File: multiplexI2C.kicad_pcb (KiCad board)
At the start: 2 copper layers, 48.3 x 71.1 mm, 59 parts, among them J1 Screw_Terminal_01x04, J17 Conn_01x04_Pin, J18 PinSocket_1x20_P2.54mm_Vertic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, J19 PinSocket_1x20_P2.54mm_Vertic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, J2 Screw_Terminal_01x04, J20 Screw_Terminal_01x02, J3 Screw_Terminal_01x04, J4 Screw_Terminal_01x04, J5 Screw_Terminal_01x04, J6 Screw_Terminal_01x04, J7 Screw_Terminal_01x04, J8 Screw_Terminal_01x04, J9 header_0.25sqmm_1x04_P4.2mm_D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, U1 TCA9548A, U2 RFM95W-915S2

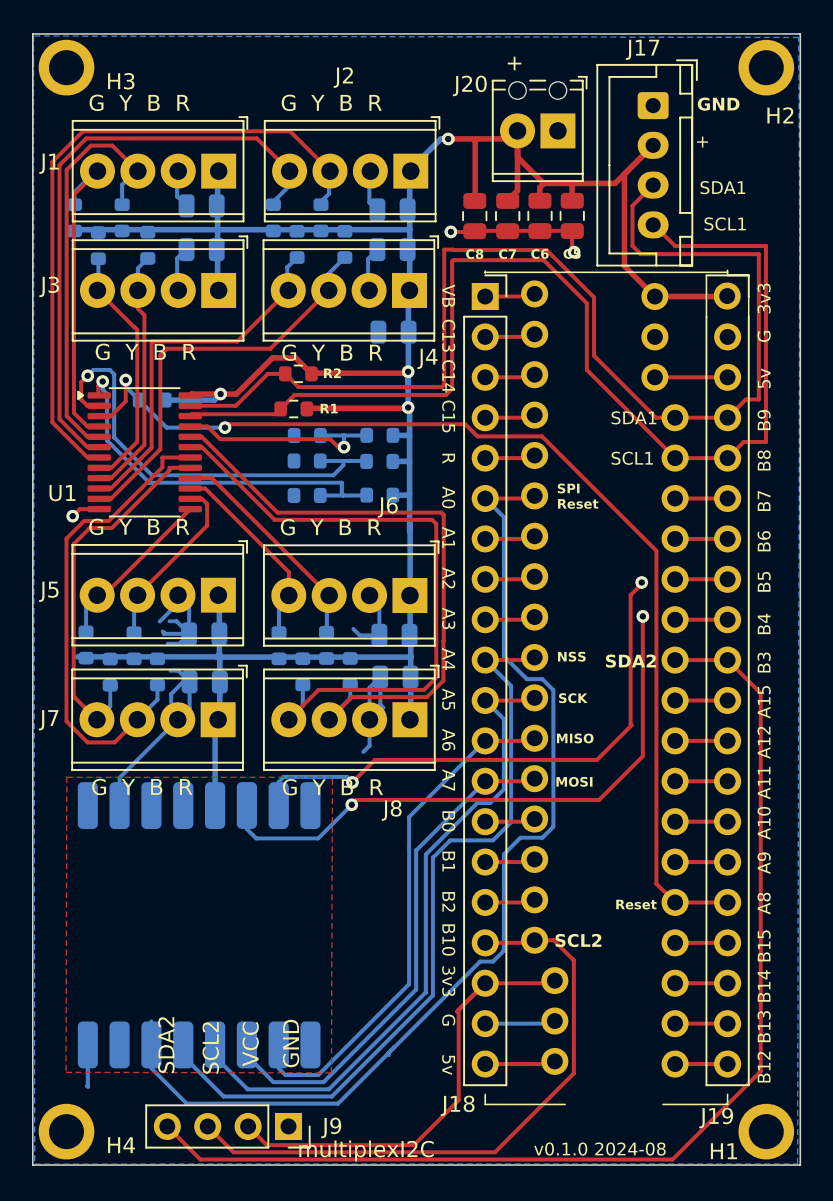
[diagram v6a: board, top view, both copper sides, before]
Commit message: DRC ot errors. 3D not showing U2.
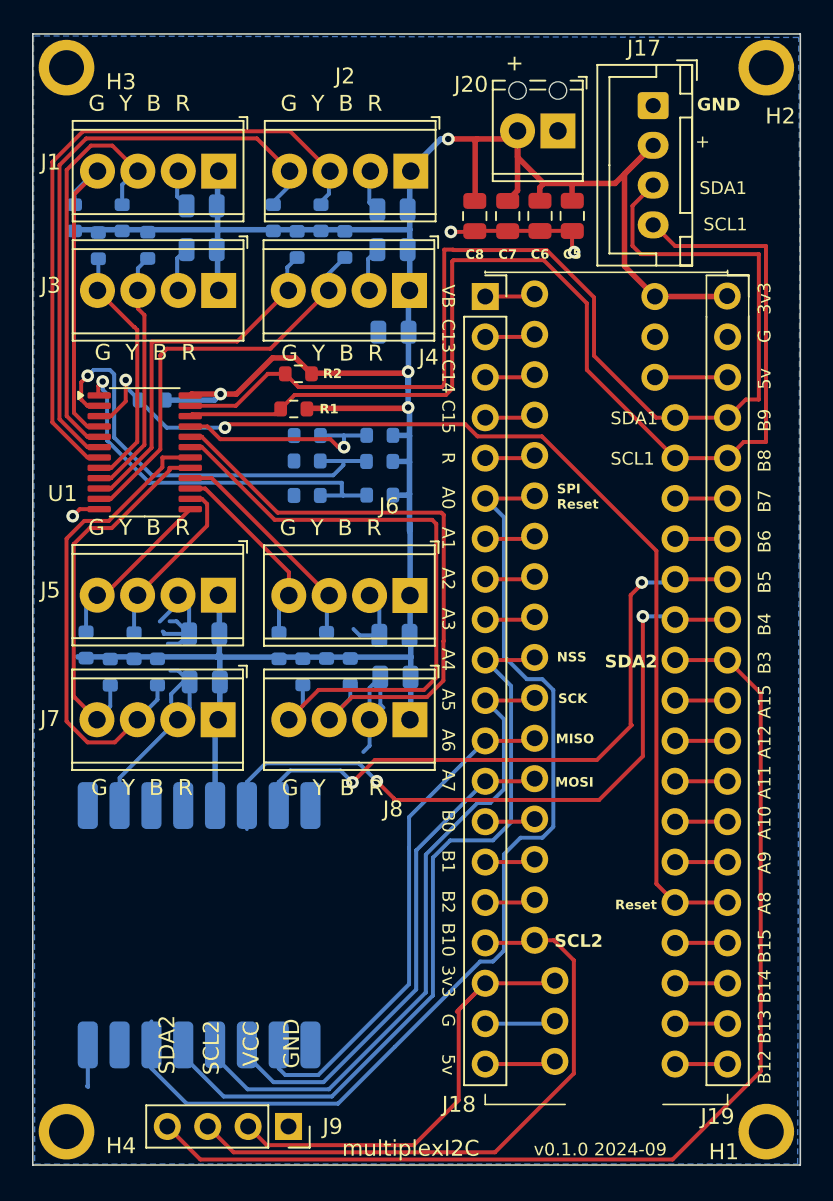
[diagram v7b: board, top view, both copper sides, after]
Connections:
- U2 pad 14: /RFM95W/DI0 -> DIO0
- U2 pad 15: /RFM95W/DI1 -> DIO1
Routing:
- net DIO0: track 3.17 -> 44.6 mm, vias 0 -> 2
- net /RFM95W/DI0: track 37.6 -> 0.00 mm, vias 2 -> 0
- net DIO1: track 3.17 -> 40.4 mm, vias 0 -> 2
- net /RFM95W/DI1: track 34.7 -> 0.00 mm, vias 2 -> 0
- net RESET: track 66.6 -> 65.9 mm
- removed copper zone on F.Cu, net GND
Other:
- board text added: "v0.1.0 2024-09"
- board text removed: "v0.1.0 2024-08"
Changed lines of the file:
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@@
 	(net 55 "/Connector1/SC")
 	(net 56 "/Connector0/SC")
-	(net 57 "/RFM95W/DI0")
-	(net 58 "unconnected-(U2-DIO4-Pad12)")
-	(net 59 "/RFM95W/DI1")
-	(net 60 "unconnected-(U2-DIO3-Pad11)")
-	(net 61 "unconnected-(U2-DIO5-Pad7)")
-	(net 62 "unconnected-(U2-DIO2-Pad16)")
-	(net 63 "unconnected-(U2-ANT-Pad9)")
-	(net 64 "DIO1")
-	(net 65 "DIO0")
+	(net 57 "unconnected-(U2-DIO4-Pad12)")
+	(net 58 "unconnected-(U2-DIO3-Pad11)")
+	(net 59 "unconnected-(U2-DIO5-Pad7)")
+	(net 60 "unconnected-(U2-DIO2-Pad16)")
+	(net 61 "unconnected-(U2-ANT-Pad9)")
+	(net 62 "DIO1")
+	(net 63 "DIO0")
 	(footprint "ProjectLib:MountingHole_2.2mm_M2_ISO7380_Pad"
 		(layer "F.Cu")
@@
 			(layers "*.Cu" "*.Mask")
 			(remove_unused_layers no)
-			(net 65 "DIO0")
+			(net 63 "DIO0")
 			(pintype "free")
 		)
@@
 			(layers "*.Cu" "*.Mask")
 			(remove_unused_layers no)
-			(net 64 "DIO1")
+			(net 62 "DIO1")
 			(pintype "free")
 		)
@@
 			(layers "*.Cu" "*.Mask")
 			(remove_unused_layers no)
-			(net 65 "DIO0")
+			(net 63 "DIO0")
 			(pinfunction "B4")
 			(pintype "bidirectional")
@@
 			(layers "*.Cu" "*.Mask")
 			(remove_unused_layers no)
-			(net 64 "DIO1")
+			(net 62 "DIO1")
 			(pinfunction "B5")
 			(pintype "bidirectional")
@@
 		(sheetname "RFM95W")
 		(sheetfile "RFM95W.kicad_sch")
-		(attr smd dnp)
+		(attr smd)
 		(fp_line
 			(start 8.1 -8.1)
@@
 			(layers "B.Cu" "B.Paste" "B.Mask")
 			(roundrect_rratio 0.25)
-			(net 61 "unconnected-(U2-DIO5-Pad7)")
+			(net 59 "unconnected-(U2-DIO5-Pad7)")
 			(pinfunction "DIO5")
 			(pintype "bidirectional+no_connect")
@@
 			(layers "B.Cu" "B.Paste" "B.Mask")
 			(roundrect_rratio 0.25)
-			(net 63 "unconnected-(U2-ANT-Pad9)")
+			(net 61 "unconnected-(U2-ANT-Pad9)")
 			(pinfunction "ANT")
 			(pintype "bidirectional+no_connect")
@@
 			(layers "B.Cu" "B.Paste" "B.Mask")
 			(roundrect_rratio 0.25)
-			(net 60 "unconnected-(U2-DIO3-Pad11)")
+			(net 58 "unconnected-(U2-DIO3-Pad11)")
 			(pinfunction "DIO3")
 			(pintype "bidirectional+no_connect")
@@
 			(layers "B.Cu" "B.Paste" "B.Mask")
 			(roundrect_rratio 0.25)
-			(net 58 "unconnected-(U2-DIO4-Pad12)")
+			(net 57 "unconnected-(U2-DIO4-Pad12)")
 			(pinfunction "DIO4")
 			(pintype "bidirectional+no_connect")
@@
 			(layers "B.Cu" "B.Paste" "B.Mask")
 			(roundrect_rratio 0.25)
-			(net 57 "/RFM95W/DI0")
+			(net 63 "DIO0")
 			(pinfunction "DIO0")
 			(pintype "bidirectional")
@@
 			(layers "B.Cu" "B.Paste" "B.Mask")
 			(roundrect_rratio 0.25)
-			(net 59 "/RFM95W/DI1")
+			(net 62 "DIO1")
 			(pinfunction "DIO1")
 			(pintype "bidirectional")
@@
 			(layers "B.Cu" "B.Paste" "B.Mask")
 			(roundrect_rratio 0.25)
-			(net 62 "unconnected-(U2-DIO2-Pad16)")
+			(net 60 "unconnected-(U2-DIO2-Pad16)")
 			(pinfunction "DIO2")
-			(pintype "bidirectional")
+			(pintype "bidirectional+no_connect")
 		)
 		(model "${KICAD8_3DMODEL_DIR}/RF_Module.3dshapes/HOPERF_RFM9XW_SMD.wrl"
@@
 		)
 	)
-	(gr_text "v0.1.0 2024-08"
+	(gr_text "v0.1.0 2024-09"
 		(at 81.026 94.742 0)
 		(layer "F.SilkS")
@@
 	)
 	(gr_text "multiplexI2C"
-		(at 66.167 94.869 0)
+		(at 68.97 94.79 0)
 		(layer "F.SilkS")
 		(effects
@@
 	)
 	(segment
-		(start 72.29 87.82)
-		(end 71.91 88.2)
-		(width 0.25)
-		(layer "B.Cu")
-		(net 19)
-	)
-	(segment
 		(start 79.153 54.515)
 		(end 79.153 63.254701)
@@
 	)
 	(segment
-		(start 71.91 88.2)
-		(end 71.91 88.34)
-		(width 0.25)
-		(layer "B.Cu")
-		(net 19)
-	)
-	(segment
 		(start 82.26 73.981701)
 		(end 81.571701 74.67)
@@
 	)
 	(segment
-		(start 85.14 72.295)
-		(end 87.89 69.545)
+		(start 90.043 58.42)
+		(end 93.218 58.42)
 		(width 0.25)
 		(layer "F.Cu")
-		(net 57)
+		(net 62)
 	)
 	(segment
-		(start 69.889694 72.295)
-		(end 85.14 72.295)
+		(start 71.04 69.78)
+		(end 85.001 69.78)
 		(width 0.25)
 		(layer "F.Cu")
-		(net 57)
+		(net 62)
 	)
 	(segment
-		(start 87.89 69.545)
-		(end 87.89 60.75)
+		(start 87.12 59.42)
+		(end 87.12 67.53)
 		(width 0.25)
 		(layer "F.Cu")
-		(net 57)
+		(net 62)
 	)
 	(segment
-		(start 69.587347 72.597347)
-		(end 69.889694 72.295)
+		(start 87.82 58.62)
+		(end 87.82 58.72)
 		(width 0.25)
 		(layer "F.Cu")
-		(net 57)
+		(net 62)
+	)
+	(segment
+		(start 87.12 67.53)
+		(end 87.1855 67.5955)
+		(width 0.25)
+		(layer "F.Cu")
+		(net 62)
+	)
+	(segment
+		(start 69.63 71.19)
+		(end 71.04 69.78)
+		(width 0.25)
+		(layer "F.Cu")
+		(net 62)
+	)
+	(segment
+		(start 87.82 58.72)
+		(end 87.12 59.42)
+		(width 0.25)
+		(layer "F.Cu")
+		(net 62)
+	)
+	(segment
+		(start 85.001 69.78)
+		(end 87.1855 67.5955)
+		(width 0.25)
+		(layer "F.Cu")
+		(net 62)
 	)
 	(via
-		(at 69.587347 72.597347)
+		(at 69.63 71.19)
 		(size 0.8)
 		(drill 0.4)
 		(layers "F.Cu" "B.Cu")
-		(net 57)
+		(net 62)
 	)
 	(via
-		(at 87.89 60.75)
+		(at 87.82 58.62)
 		(size 0.8)
 		(drill 0.4)
 		(layers "F.Cu" "B.Cu")
-		(net 57)
+		(net 62)
 	)
 	(segment
-		(start 62.99 74.12)
-		(end 63.581802 74.711802)
+		(start 64.99 71.17)
+		(end 64.99 72.645)
 		(width 0.25)
 		(layer "B.Cu")
-		(net 57)
+		(net 62)
 	)
 	(segment
-		(start 63.581802 74.711802)
-		(end 67.472892 74.711802)
+		(start 69.63 71.19)
+		(end 68.88 70.44)
 		(width 0.25)
 		(layer "B.Cu")
-		(net 57)
+		(net 62)
 	)
 	(segment
-		(start 62.99 72.645)
-		(end 62.99 74.12)
+		(start 87.82 58.62)
+		(end 89.716 58.62)
 		(width 0.25)
 		(layer "B.Cu")
-		(net 57)
+		(net 62)
 	)
 	(segment
-		(start 67.472892 74.711802)
-		(end 69.587347 72.597347)
+		(start 65.72 70.44)
+		(end 64.99 71.17)
 		(width 0.25)
 		(layer "B.Cu")
-		(net 57)
+		(net 62)
 	)
 	(segment
-		(start 71.04 69.78)
-		(end 85.001 69.78)
+		(start 69.63 71.19)
+		(end 69.63 71.18)
 		(width 0.25)
-		(layer "F.Cu")
-		(net 59)
+		(layer "B.Cu")
+		(net 62)
 	)
 	(segment
-		(start 87.12 59.42)
-		(end 87.12 67.53)
+		(start 89.716 58.62)
+		(end 89.916 58.42)
+		(width 0.25)
+		(layer "B.Cu")
+		(net 62)
+	)
+	(segment
+		(start 68.88 70.44)
+		(end 65.72 70.44)
+		(width 0.25)
+		(layer "B.Cu")
+		(net 62)
+	)
+	(segment
+		(start 72.24 72.295)
+		(end 85.14 72.295)
 		(width 0.25)
 		(layer "F.Cu")
-		(net 59)
+		(net 63)
 	)
 	(segment
-		(start 87.82 58.62)
-		(end 87.82 58.72)
+		(start 85.14 72.295)
+		(end 87.89 69.545)
 		(width 0.25)
 		(layer "F.Cu")
-		(net 59)
+		(net 63)
 	)
 	(segment
-		(start 87.12 67.53)
-		(end 87.1855 67.5955)
+		(start 90.043 60.96)
+		(end 93.218 60.96)
 		(width 0.25)
 		(layer "F.Cu")
-		(net 59)
+		(net 63)
 	)
 	(segment
-		(start 69.63 71.19)
-		(end 71.04 69.78)
+		(start 72.24 72.2)
+		(end 72.24 72.295)
 		(width 0.25)
 		(layer "F.Cu")
-		(net 59)
+		(net 63)
 	)
 	(segment
-		(start 87.82 58.72)
-		(end 87.12 59.42)
+		(start 87.89 69.545)
+		(end 87.89 60.75)
 		(width 0.25)
 		(layer "F.Cu")
-		(net 59)
+		(net 63)
 	)
 	(segment
-		(start 85.001 69.78)
-		(end 87.1855 67.5955)
+		(start 71.16 71.12)
+		(end 72.24 72.2)
 		(width 0.25)
 		(layer "F.Cu")
-		(net 59)
+		(net 63)
 	)
 	(via
-		(at 69.63 71.19)
+		(at 71.16 71.12)
 		(size 0.8)
 		(drill 0.4)
 		(layers "F.Cu" "B.Cu")
-		(net 59)
+		(net 63)
 	)
 	(via
-		(at 87.82 58.62)
+		(at 87.89 60.75)
 		(size 0.8)
 		(drill 0.4)
 		(layers "F.Cu" "B.Cu")
-		(net 59)
+		(net 63)
 	)
 	(segment
-		(start 64.99 72.645)
-		(end 64.99 71.17)
+		(start 87.89 60.75)
+		(end 89.706 60.75)
 		(width 0.25)
 		(layer "B.Cu")
-		(net 59)
+		(net 63)
 	)
 	(segment
-		(start 69.285 70.845)
-		(end 69.63 71.19)
+		(start 64.17 69.99)
+		(end 62.99 71.17)
 		(width 0.25)
 		(layer "B.Cu")
-		(net 59)
+		(net 63)
 	)
 	(segment
-		(start 64.99 71.17)
-		(end 65.315 70.845)
+		(start 89.706 60.75)
+		(end 89.916 60.96)
 		(width 0.25)
 		(layer "B.Cu")
-		(net 59)
+		(net 63)
 	)
 	(segment
-		(start 65.315 70.845)
-		(end 69.285 70.845)
+		(start 71.16 71.12)
+		(end 70.03 69.99)
 		(width 0.25)
 		(layer "B.Cu")
-		(net 59)
+		(net 63)
 	)
 	(segment
-		(start 90.043 58.42)
-		(end 93.218 58.42)
+		(start 62.99 72.645)
+		(end 62.99 74.12)
 		(width 0.25)
-		(layer "F.Cu")
-		(net 64)
+		(layer "B.Cu")
+		(net 63)
 	)
 	(segment
-		(start 90.043 60.96)
-		(end 93.218 60.96)
+		(start 62.99 71.17)
+		(end 62.99 72.645)
 		(width 0.25)
-		(layer "F.Cu")
-		(net 65)
+		(layer "B.Cu")
+		(net 63)
 	)
-	(zone
-		(net 2)
-		(net_name "GND")
-		(layer "F.Cu")
-		(hatch edge 0.5)
-		(priority 1)
-		(connect_pads
-			(clearance 0.29)
-		)
-		(min_thickness 0.25)
-		(filled_areas_thickness no)
-		(fill yes
-			(thermal_gap 0.5)
-			(thermal_bridge_width 0.5)
-		)
-		(polygon
-			(pts
-				(xy 51.67 70.84) (xy 51.62 89.42) (xy 68.31 89.46) (xy 68.37 70.87) (xy 51.69 70.87) (xy 51.66 70.89)
-			)
-		)
+	(segment
+		(start 70.03 69.99)
+		(end 64.17 69.99)
+		(width 0.25)
+		(layer "B.Cu")
+		(net 63)
 	)
 	(zone

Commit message: added antenna connector.
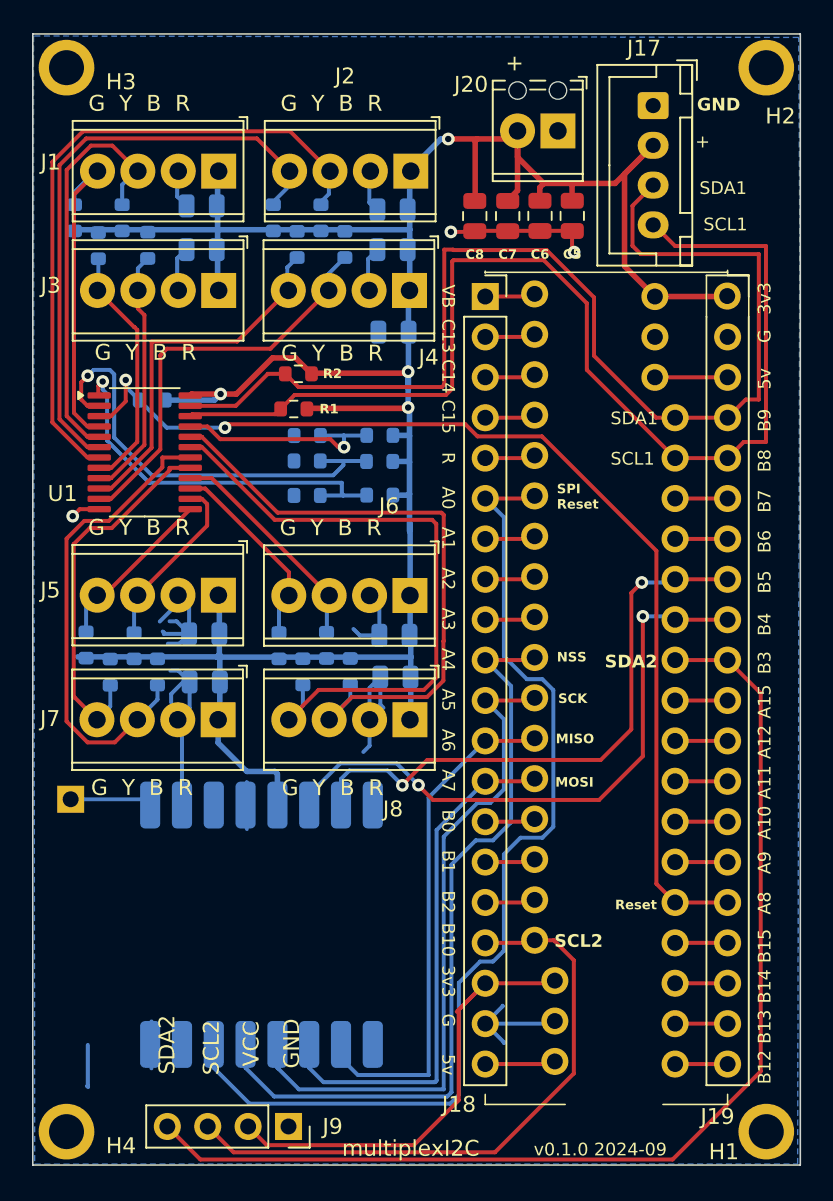
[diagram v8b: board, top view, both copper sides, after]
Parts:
- added AE1: Antenna, ProjectLib:PinSocket_1x01_P2.54mm_Horizontal, B.Cu at (51.9, 72.2)
- moved U2 3.92 mm to (63.9, 80.1)
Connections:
- U2 pad 9: unconnected-(U2-ANT-Pad9) -> ANT
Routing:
- net DIO0: track 44.6 -> 38.6 mm
- net ANT: track 0.00 -> 5.29 mm
- net GND: track 61.9 -> 66.7 mm
- net +3V3: track 171.9 -> 176.1 mm
- net DIO1: track 40.4 -> 36.9 mm
- net unconnected-(U2-DIO4-Pad12): track 0.00 -> 2.95 mm
- net SCK: track 41.8 -> 44.0 mm
- net unconnected-(U2-DIO5-Pad7): track 0.00 -> 0.71 mm
- net MOSI: track 32.4 -> 33.0 mm
- net NSS: track 48.5 -> 49.0 mm
- net RESET: track 65.9 -> 65.4 mm
